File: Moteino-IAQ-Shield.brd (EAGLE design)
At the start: 33.3 x 23.1 mm, 15 parts, among them J3 USB-MICROB, U1 CCS811, U10 TSL2591, U2 SHT35

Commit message: Trace and component adjustments
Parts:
- moved U1 1.02 mm to (23.9, 8.64)
- moved R2 0.91 mm to (26.2, 10.2)
- moved C5 0.86 mm to (23.7, 4.60)
- moved C16 0.20 mm to (30.6, 14.4)
- moved U2 0.15 mm to (30.4, 17.3)
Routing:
- net GND: track 2.51 -> 4.55 mm, vias 7 -> 11
- net D6: track 15.5 -> 16.5 mm
- net VCC: track 63.4 -> 64.2 mm
- net A4_SDA: track 36.1 -> 36.9 mm

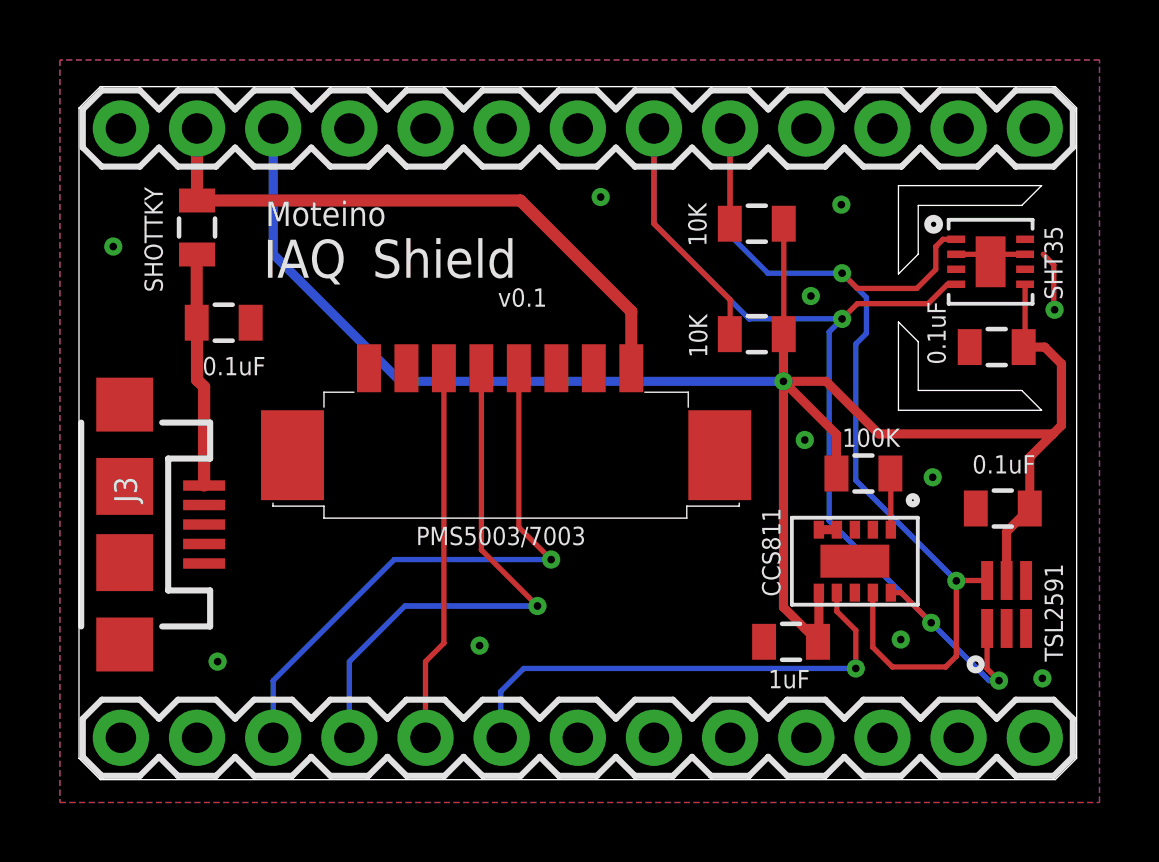
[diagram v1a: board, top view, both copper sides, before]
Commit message: Updated library for Molex connector
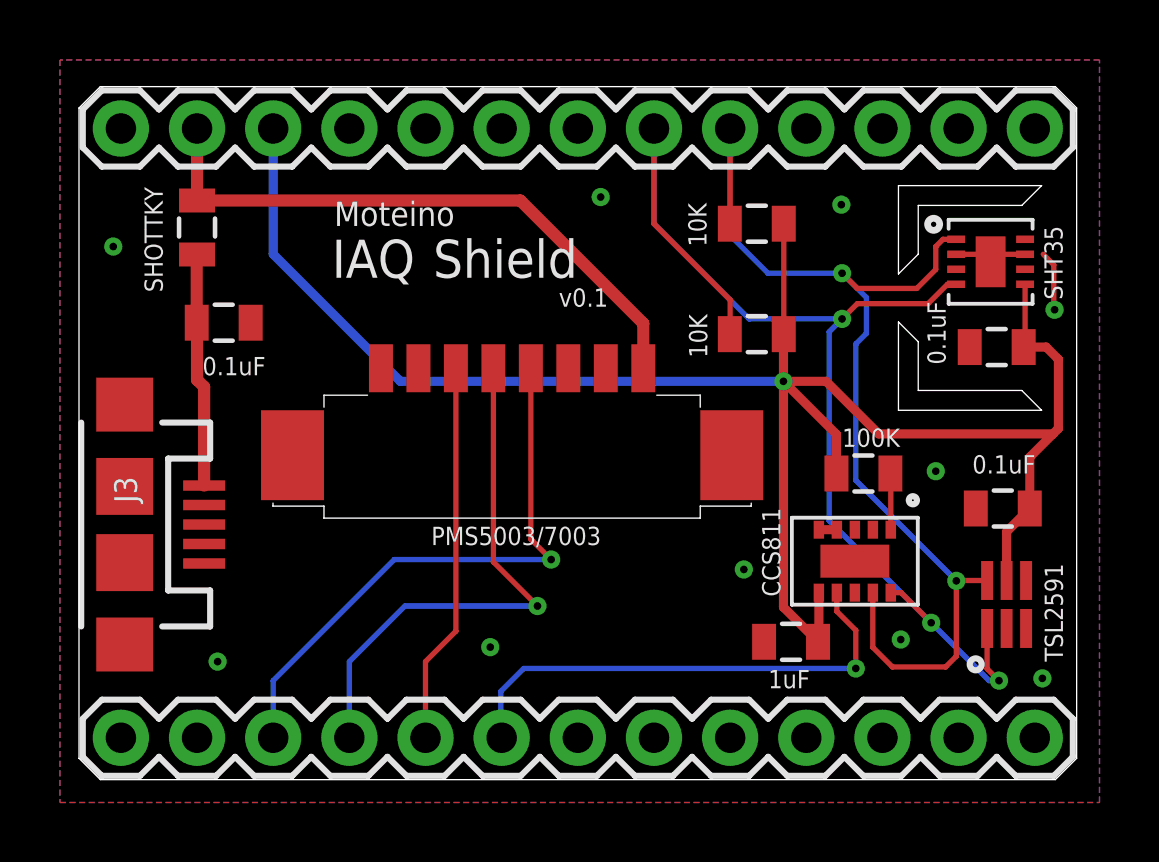
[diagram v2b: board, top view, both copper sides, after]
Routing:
- net GND: vias 11 -> 10
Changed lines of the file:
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@@
 <setting verticaltext="up"/>
 </settings>
-<grid distance="2" unitdist="mil" unit="mil" style="lines" multiple="1" display="yes" altdistance="0.1" altunitdist="mm" altunit="mm"/>
+<grid distance="10" unitdist="mil" unit="mil" style="lines" multiple="1" display="yes" altdistance="0.1" altunitdist="mm" altunit="mm"/>
 <layers>
 <layer number="1" name="Top" color="4" fill="1" visible="yes" active="yes"/>
@@
 <wire x1="31.4452" y1="12.9794" x2="27.9908" y2="12.9794" width="0.0254" layer="20"/>
 <wire x1="27.9908" y1="12.9794" x2="27.9908" y2="14.605" width="0.0254" layer="20"/>
-<text x="6.223" y="18.4658" size="0.8128" layer="21" font="vector">Moteino</text>
-<text x="6.1468" y="16.7386" size="1.27" layer="21" font="vector" ratio="15">IAQ</text>
-<text x="9.779" y="16.7386" size="1.27" layer="21" font="vector">Shield</text>
-<text x="13.97" y="15.7734" size="0.6096" layer="21" font="vector">v0.1</text>
+<text x="8.509" y="18.4658" size="0.8128" layer="21" font="vector">Moteino</text>
+<text x="8.4328" y="16.7386" size="1.27" layer="21" font="vector" ratio="15">IAQ</text>
+<text x="11.811" y="16.7386" size="1.27" layer="21" font="vector">Shield</text>
+<text x="16.002" y="15.7734" size="0.6096" layer="21" font="vector">v0.1</text>
 <text x="17.272" y="10.287" size="0.6096" layer="22" font="vector" rot="MR0" align="bottom-center">Designed by AKstudios
 April 2017</text>
-<text x="14.0716" y="7.8232" size="0.6096" layer="21" font="vector" align="bottom-center">PMS5003/7003</text>
+<text x="14.5796" y="7.8232" size="0.6096" layer="21" font="vector" align="bottom-center">PMS5003/7003</text>
 </plain>
 <attributes>
@@
 <wire x1="30.8062" y1="17.522" x2="30.4038" y2="17.272" width="0.1778" layer="1"/>
 <via x="4.6228" y="3.937" extent="1-16" drill="0.254" diameter="0.127"/>
-<via x="13.3604" y="4.4704" extent="1-16" drill="0.254" diameter="0.127"/>
+<via x="13.716" y="4.4196" extent="1-16" drill="0.254" diameter="0.127"/>
 <via x="1.143" y="17.78" extent="1-16" drill="0.254" diameter="0.127"/>
 <contactref element="C11" pad="2"/>
@@
 <contactref element="U1" pad="11"/>
 <contactref element="C5" pad="2"/>
-<via x="28.4734" y="10.0838" extent="1-16" drill="0.254" diameter="0.127"/>
+<via x="28.575" y="10.287" extent="1-16" drill="0.254" diameter="0.127"/>
 <via x="32.131" y="3.3782" extent="1-16" drill="0.254" diameter="0.127"/>
-<via x="24.2062" y="11.3284" extent="1-16" drill="0.254" diameter="0.127"/>
+<via x="22.1742" y="7.0104" extent="1-16" drill="0.254" diameter="0.127"/>
 <via x="27.4066" y="4.6736" extent="1-16" drill="0.254" diameter="0.127"/>
 <via x="32.5374" y="15.6718" extent="1-16" drill="0.254" diameter="0.127"/>
 <via x="25.4254" y="19.177" extent="1-16" drill="0.254" diameter="0.127"/>
-<via x="24.4094" y="16.129" extent="1-16" drill="0.254" diameter="0.127"/>
 <wire x1="32.1604" y1="17.522" x2="32.512" y2="17.1704" width="0.1778" layer="1"/>
 <wire x1="32.512" y1="17.1704" x2="32.512" y2="15.6972" width="0.1778" layer="1"/>
 <wire x1="32.512" y1="15.6972" x2="32.5374" y2="15.6718" width="0.1778" layer="1"/>
-<wire x1="32.1604" y1="17.522" x2="31.5538" y2="17.522" width="0" layer="19" extent="1-1"/>
+<wire x1="31.5538" y1="17.522" x2="32.1604" y2="17.522" width="0" layer="19" extent="1-1"/>
 </signal>
 <signal name="D10_SS">
@@
 <contactref element="U$1" pad="P$9"/>
 <contactref element="R11" pad="1"/>
-<wire x1="18.4206" y1="15.6154" x2="18.4206" y2="13.7218" width="0.4064" layer="1"/>
 <wire x1="3.937" y1="21.717" x2="3.937" y2="19.315" width="0.4064" layer="1"/>
-<wire x1="3.937" y1="19.315" x2="14.721" y2="19.315" width="0.4064" layer="1"/>
-<wire x1="14.721" y1="19.315" x2="18.4206" y2="15.6154" width="0.4064" layer="1"/>
+<wire x1="14.721" y1="19.315" x2="3.937" y2="19.315" width="0.4064" layer="1"/>
+<wire x1="18.8206" y1="13.7218" x2="18.8206" y2="15.2154" width="0.4064" layer="1"/>
+<wire x1="18.8206" y1="15.2154" x2="14.721" y2="19.315" width="0.4064" layer="1"/>
 </signal>
 <signal name="VCC">
@@
 <wire x1="24.9174" y1="13.2842" x2="26.67" y2="11.5316" width="0.3048" layer="1"/>
 <wire x1="26.67" y1="11.5316" x2="32.4866" y2="11.5316" width="0.3048" layer="1"/>
-<wire x1="32.4866" y1="11.5316" x2="32.766" y2="11.811" width="0.3048" layer="1"/>
 <wire x1="25.262" y1="11.5172" x2="23.495" y2="13.2842" width="0.3048" layer="1"/>
 <wire x1="31.5538" y1="16.522" x2="31.5538" y2="14.474" width="0.1778" layer="1"/>
-<wire x1="31.507" y1="14.4272" x2="31.5538" y2="14.474" width="0.1778" layer="1"/>
-<wire x1="32.766" y1="11.811" x2="32.766" y2="13.8684" width="0.3048" layer="1"/>
-<wire x1="32.766" y1="13.8684" x2="32.2072" y2="14.4272" width="0.3048" layer="1"/>
-<wire x1="32.2072" y1="14.4272" x2="31.507" y2="14.4272" width="0.3048" layer="1"/>
+<wire x1="31.5538" y1="14.474" x2="31.507" y2="14.4272" width="0.1778" layer="1"/>
+<wire x1="32.258" y1="14.4272" x2="32.6644" y2="14.0208" width="0.3048" layer="1"/>
+<wire x1="32.6644" y1="14.0208" x2="32.6644" y2="11.7094" width="0.3048" layer="1"/>
+<wire x1="32.6644" y1="11.7094" x2="32.4866" y2="11.5316" width="0.3048" layer="1"/>
+<wire x1="31.507" y1="14.4272" x2="32.258" y2="14.4272" width="0.3048" layer="1"/>
 </signal>
 <signal name="D9">
@@
 <contactref element="DIGITALSIDE" pad="9"/>
 <contactref element="U$1" pad="P$4"/>
-<wire x1="12.1706" y1="13.7218" x2="12.1706" y2="4.5506" width="0.1778" layer="1"/>
-<wire x1="12.1706" y1="4.5506" x2="11.557" y2="3.937" width="0.1778" layer="1"/>
 <wire x1="11.557" y1="3.937" x2="11.557" y2="1.397" width="0.1778" layer="1"/>
+<wire x1="12.5706" y1="13.7218" x2="12.5706" y2="4.9506" width="0.1778" layer="1"/>
+<wire x1="12.5706" y1="4.9506" x2="11.557" y2="3.937" width="0.1778" layer="1"/>
 </signal>
 <signal name="D4">
@@
 <via x="15.2908" y="5.7912" extent="1-16" drill="0.254" diameter="0.127"/>
 <wire x1="9.017" y1="1.397" x2="9.017" y2="3.937" width="0.1778" layer="16"/>
-<wire x1="13.4206" y1="13.7218" x2="13.4206" y2="7.6614" width="0.1778" layer="1"/>
-<wire x1="13.4206" y1="7.6614" x2="15.2908" y2="5.7912" width="0.1778" layer="1"/>
 <wire x1="9.017" y1="3.937" x2="10.8712" y2="5.7912" width="0.1778" layer="16"/>
 <wire x1="10.8712" y1="5.7912" x2="15.2908" y2="5.7912" width="0.1778" layer="16"/>
+<wire x1="13.8206" y1="13.7218" x2="13.8206" y2="7.2614" width="0.1778" layer="1"/>
+<wire x1="13.8206" y1="7.2614" x2="15.2908" y2="5.7912" width="0.1778" layer="1"/>
 </signal>
 <signal name="D3">
@@
 <via x="15.748" y="7.3406" extent="1-16" drill="0.254" diameter="0.127"/>
 <wire x1="6.477" y1="3.302" x2="6.477" y2="1.397" width="0.1778" layer="16"/>
-<wire x1="14.6706" y1="13.7218" x2="14.6706" y2="8.418" width="0.1778" layer="1"/>
 <wire x1="15.748" y1="7.3406" x2="10.5156" y2="7.3406" width="0.1778" layer="16"/>
 <wire x1="10.5156" y1="7.3406" x2="6.477" y2="3.302" width="0.1778" layer="16"/>
-<wire x1="14.6706" y1="8.418" x2="15.748" y2="7.3406" width="0.1778" layer="1"/>
+<wire x1="15.0706" y1="13.7218" x2="15.0706" y2="8.018" width="0.1778" layer="1"/>
+<wire x1="15.0706" y1="8.018" x2="15.748" y2="7.3406" width="0.1778" layer="1"/>
 </signal>
 <signal name="D1_TX">

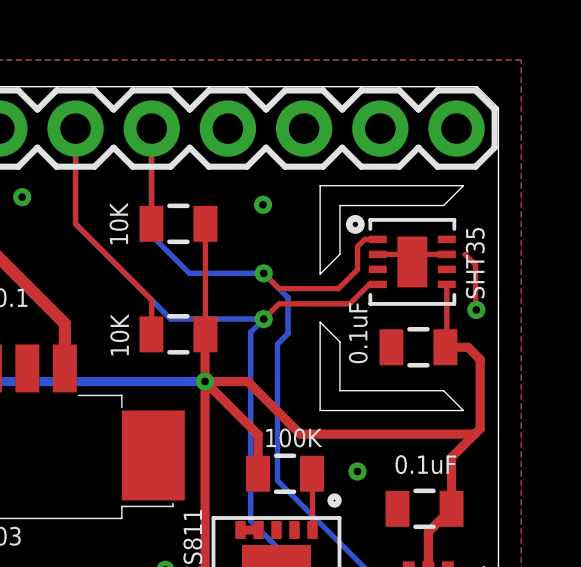
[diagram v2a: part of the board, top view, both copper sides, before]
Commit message: Connected GND trace for SHT sensor
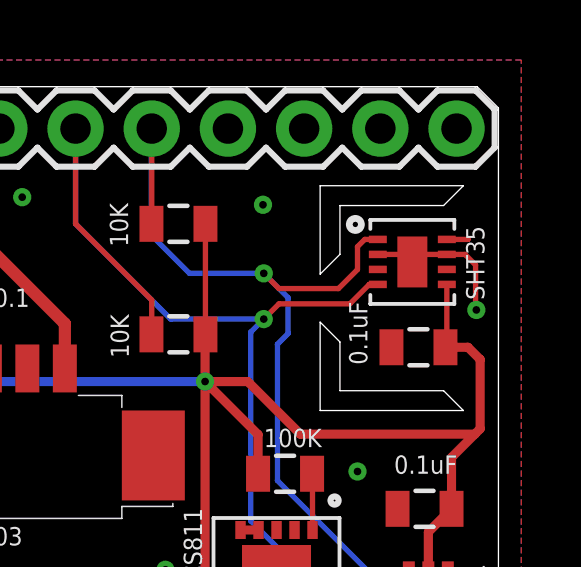
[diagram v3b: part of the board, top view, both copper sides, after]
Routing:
- net GND: track 4.55 -> 5.87 mm
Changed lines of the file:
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@@
 <?xml version="1.0" encoding="utf-8"?>
 <!DOCTYPE eagle SYSTEM "eagle.dtd">
-<eagle version="8.1.0">
+<eagle version="8.1.1">
 <drawing>
 <settings>
@@
 <wire x1="29.2538" y1="17.522" x2="30.3062" y2="17.522" width="0.1778" layer="1"/>
 <wire x1="30.4038" y1="17.272" x2="30.3062" y2="17.522" width="0.1778" layer="1"/>
-<wire x1="30.8062" y1="17.522" x2="31.5538" y2="17.522" width="0.1778" layer="1"/>
+<wire x1="31.5538" y1="17.522" x2="30.8062" y2="17.522" width="0.1778" layer="1"/>
 <wire x1="30.8062" y1="17.522" x2="30.4038" y2="17.272" width="0.1778" layer="1"/>
 <via x="4.6228" y="3.937" extent="1-16" drill="0.254" diameter="0.127"/>
@@
 <via x="32.5374" y="15.6718" extent="1-16" drill="0.254" diameter="0.127"/>
 <via x="25.4254" y="19.177" extent="1-16" drill="0.254" diameter="0.127"/>
-<wire x1="32.1604" y1="17.522" x2="32.512" y2="17.1704" width="0.1778" layer="1"/>
+<wire x1="32.512" y1="17.1704" x2="32.1604" y2="17.522" width="0.1778" layer="1"/>
 <wire x1="32.512" y1="17.1704" x2="32.512" y2="15.6972" width="0.1778" layer="1"/>
 <wire x1="32.512" y1="15.6972" x2="32.5374" y2="15.6718" width="0.1778" layer="1"/>
-<wire x1="31.5538" y1="17.522" x2="32.1604" y2="17.522" width="0" layer="19" extent="1-1"/>
+<wire x1="32.1604" y1="17.522" x2="31.5538" y2="17.522" width="0.1778" layer="1"/>
+<wire x1="31.5538" y1="18.022" x2="32.258" y2="18.022" width="0.1778" layer="1"/>
+<wire x1="32.258" y1="18.022" x2="32.258" y2="18.034" width="0.1778" layer="1"/>
 </signal>
 <signal name="D10_SS">
